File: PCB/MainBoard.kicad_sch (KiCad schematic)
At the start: 15 parts, among them U2 ATmega2560-16A, Y1 Crystal_GND24

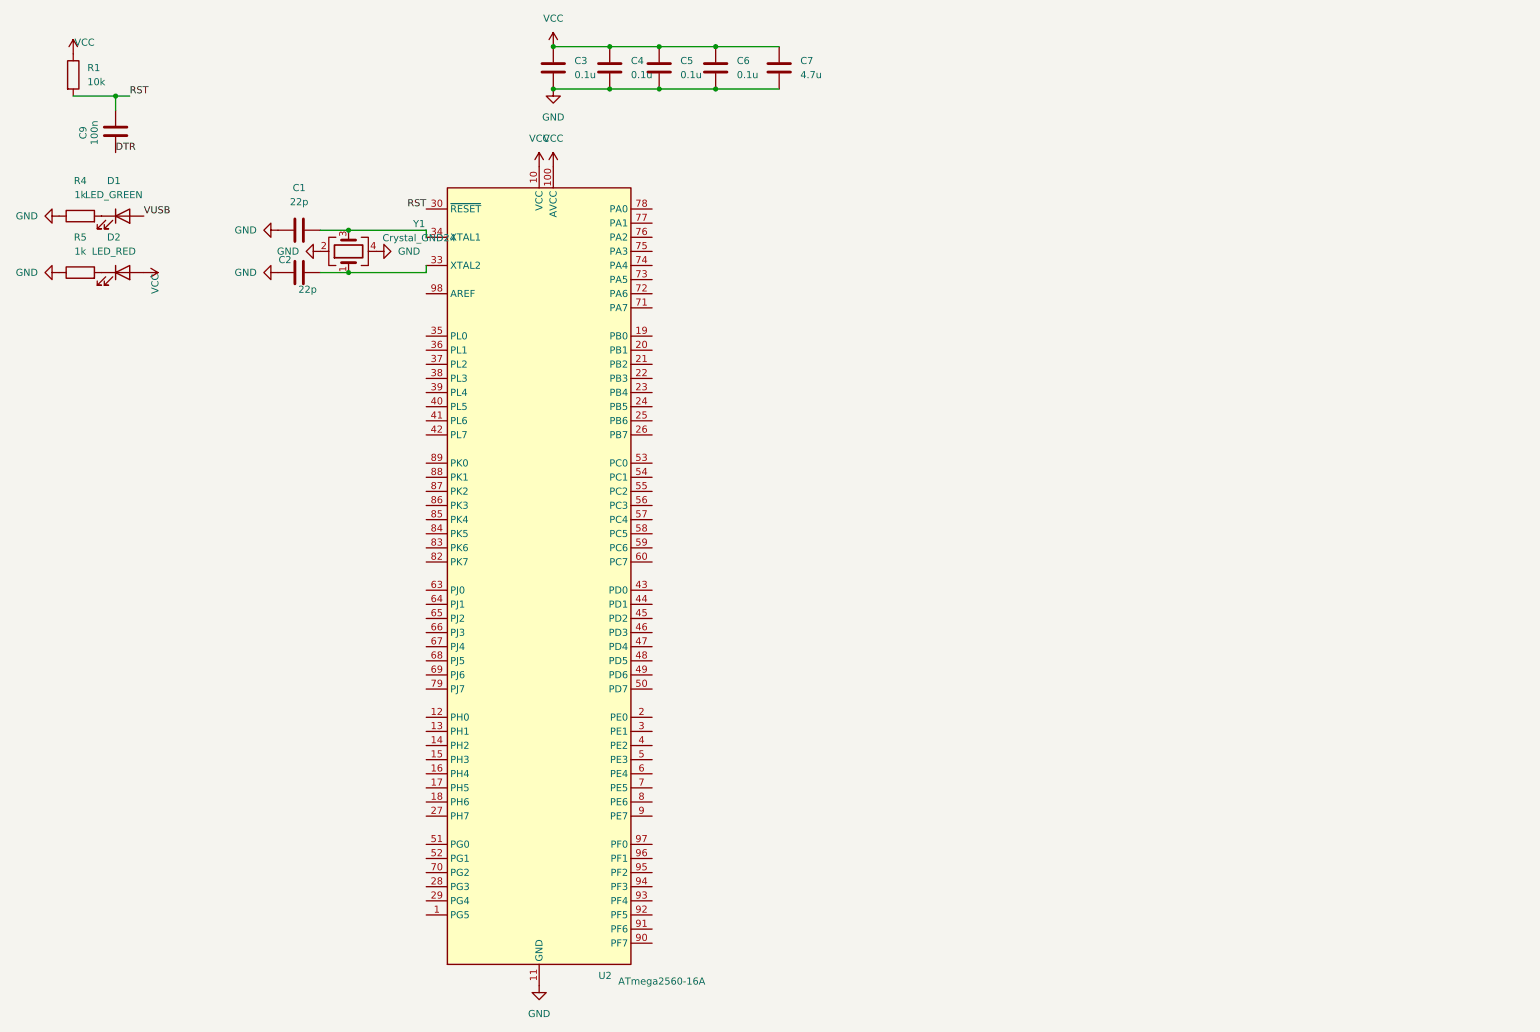
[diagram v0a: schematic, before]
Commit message: Updated board with the right hall effect analog sensor and some ADCs. Considering reducing the MCU.
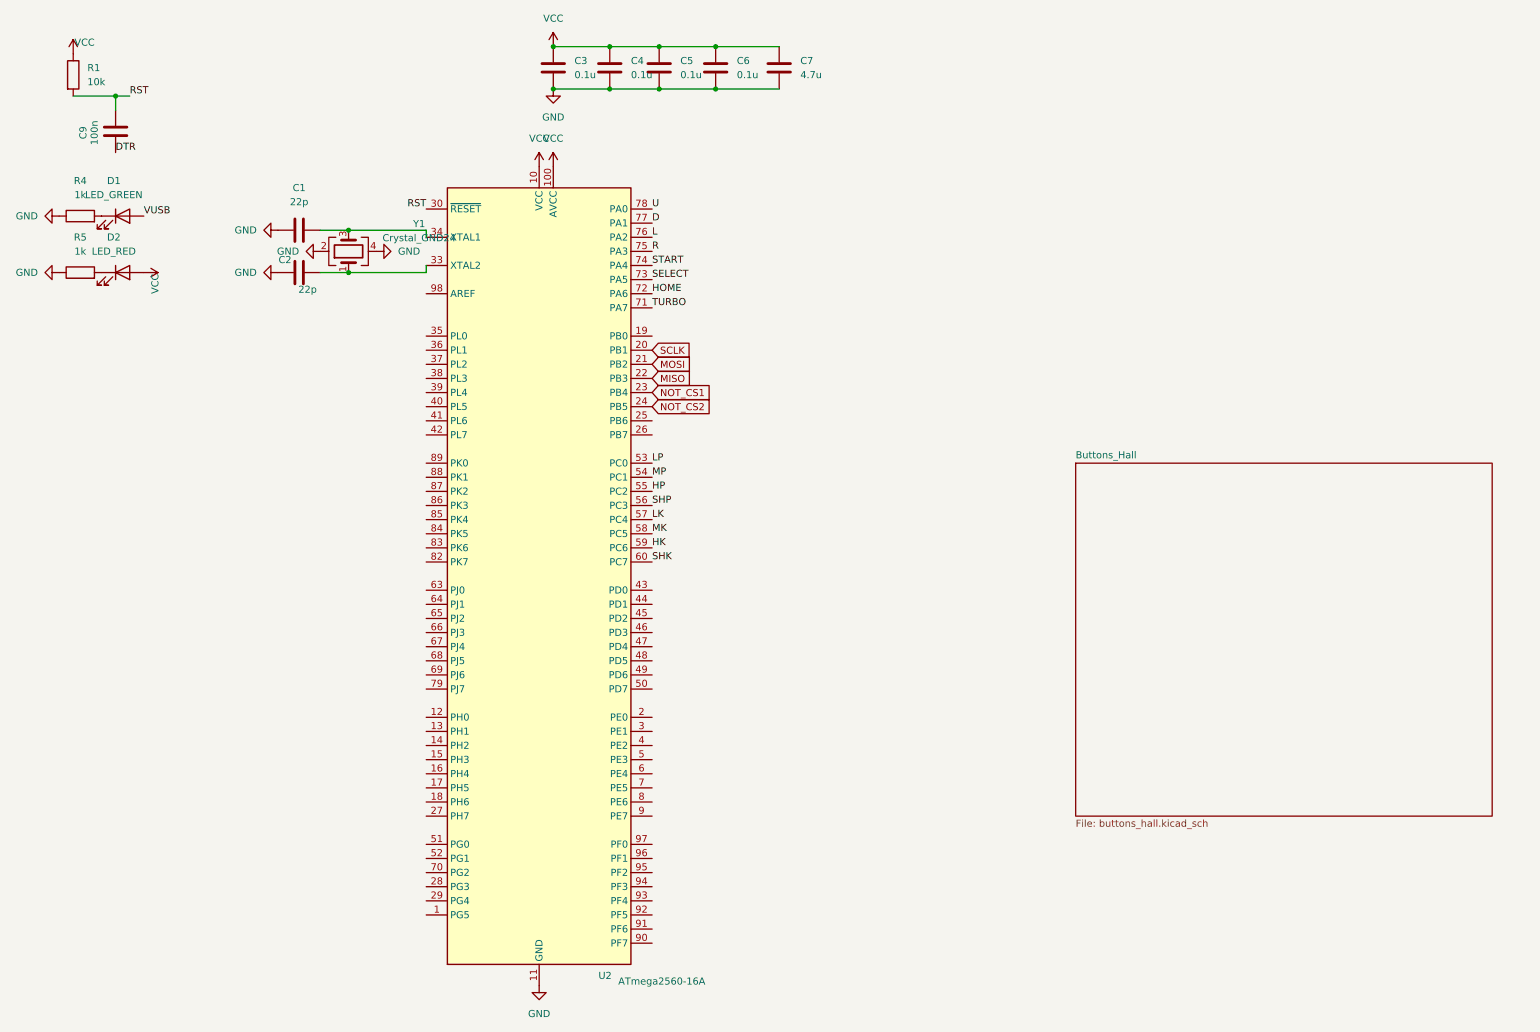
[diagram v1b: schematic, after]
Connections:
- net SCLK: now reaches U2.20 (PB1)
- net MOSI: now reaches U2.21 (PB2)
- net MISO: now reaches U2.22 (PB3)
- net NOT_CS1: now reaches U2.23 (PB4)
- net NOT_CS2: now reaches U2.24 (PB5)
- net LP: now reaches U2.53 (PC0)
- net MP: now reaches U2.54 (PC1)
- net HP: now reaches U2.55 (PC2)
- net SHP: now reaches U2.56 (PC3)
- net LK: now reaches U2.57 (PC4)
- net MK: now reaches U2.58 (PC5)
- net HK: now reaches U2.59 (PC6)
- net SHK: now reaches U2.60 (PC7)
- net TURBO: now reaches U2.71 (PA7)
- net HOME: now reaches U2.72 (PA6)
- net SELECT: now reaches U2.73 (PA5)
- net START: now reaches U2.74 (PA4)
- net R: now reaches U2.75 (PA3)
- net L: now reaches U2.76 (PA2)
- net D: now reaches U2.77 (PA1)
- net U: now reaches U2.78 (PA0)
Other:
- added sheet Buttons_Hall (buttons_hall.kicad_sch)

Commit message: Worked on schematic, added USB-C, worked on pcb
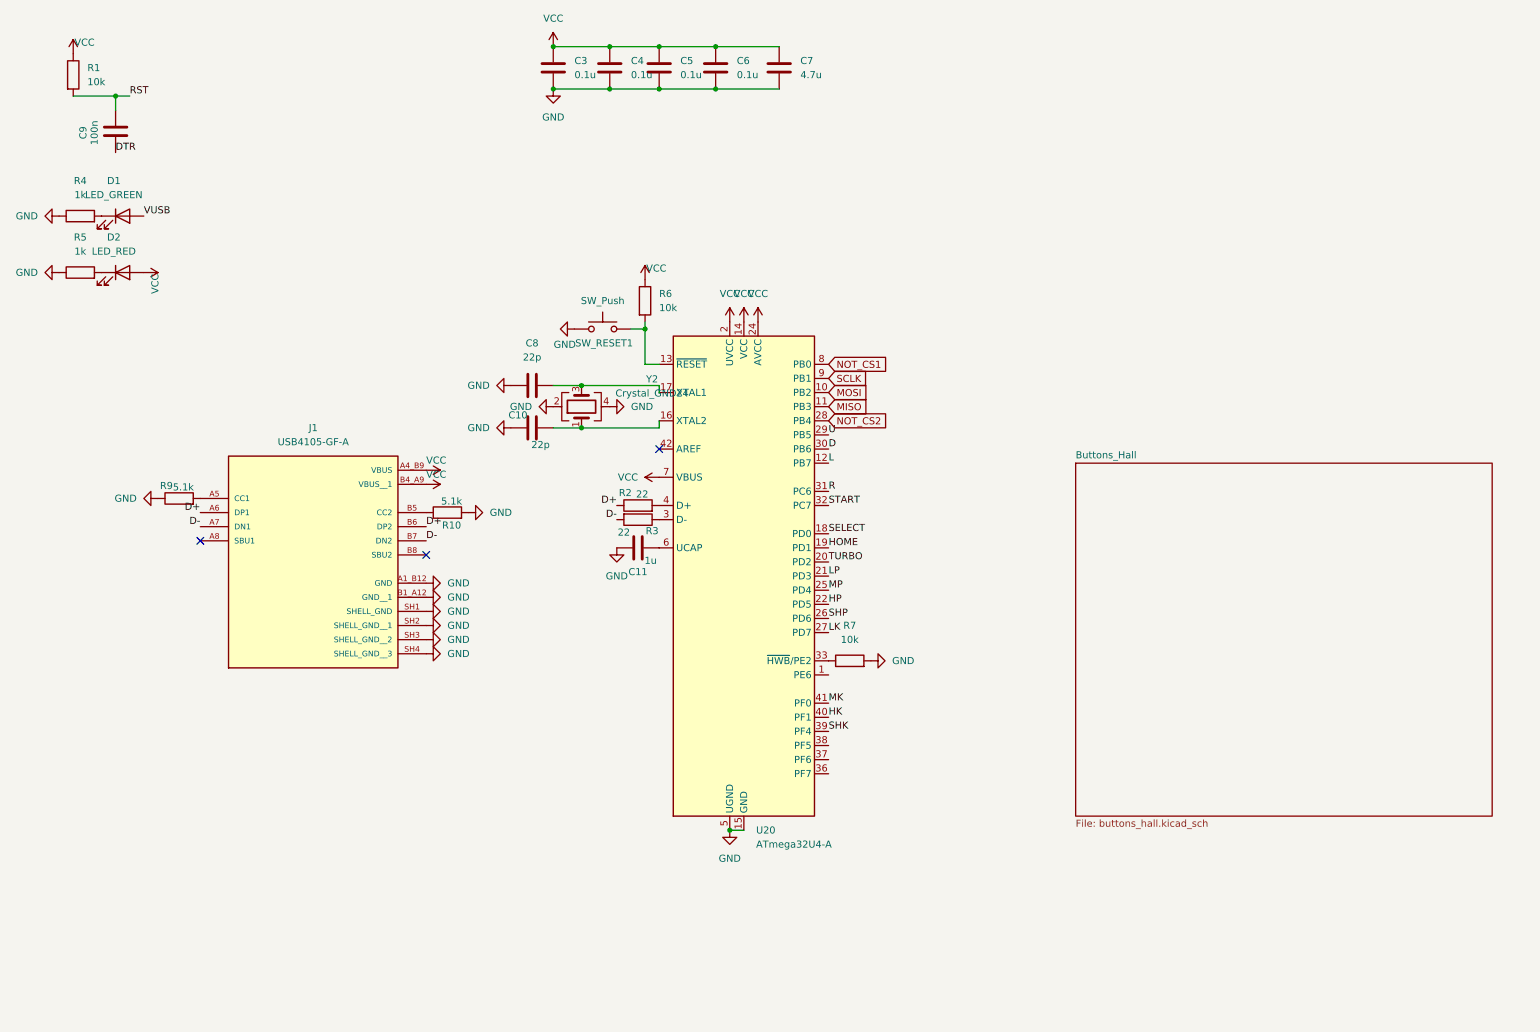
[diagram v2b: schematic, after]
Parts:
- removed C1, C2: 22p, Capacitor_SMD:C_0603_1608Metric, symbol Device:C
- removed U2: ATmega2560-16A, Package_QFP:TQFP-100_14x14mm_P0.5mm, symbol MCU_Microchip_ATmega:ATmega2560-16A
- removed Y1: Crystal_GND24, Crystal:Crystal_SMD_SeikoEpson_FA238-4Pin_3.2x2.5mm, symbol Device:Crystal_GND24
- added C10, C8: 22p, Capacitor_SMD:C_0603_1608Metric, symbol Device:C
- added C11: 1u, Capacitor_SMD:C_0603_1608Metric, symbol Device:C
- added J1: USB4105-GF-A, USB4105_GF_A:GCT_USB4105-GF-A, symbol USB4105-GF-A:USB4105-GF-A
- added R10, R9: 5.1k, Resistor_SMD:R_0603_1608Metric, symbol Device:R
- added R2, R3: 22, Resistor_SMD:R_0603_1608Metric, symbol Device:R
- added R6, R7: 10k, Resistor_SMD:R_0603_1608Metric, symbol Device:R
- added SW_RESET1: SW_Push, Button_Switch_SMD:SW_SPST_TL3342, symbol Switch:SW_Push
- added U20: ATmega32U4-A, Package_QFP:TQFP-44_10x10mm_P0.8mm, symbol MCU_Microchip_ATmega:ATmega32U4-A
- added Y2: Crystal_GND24, Crystal:Crystal_SMD_SeikoEpson_FA238-4Pin_3.2x2.5mm, symbol Device:Crystal_GND24
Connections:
- net D: now also U20.30 (PB6)
- net GND: now also C10.1, C11.1, C8.1, J1.A1_B12 (GND), J1.B1_A12 (GND__1), J1.SH1 (SHELL_GND), J1.SH2 (SHELL_GND__1), J1.SH3 (SHELL_GND__2), J1.SH4 (SHELL_GND__3), R10.2, R7.2, R9.1, SW_RESET1.1, U20.15 (GND), U20.23 (GND), U20.35 (GND), U20.43 (GND), U20.5 (UGND), Y2.2, Y2.4
- net HK: now also U20.40 (PF1)
- net HOME: now also U20.19 (PD1)
- net HP: now also U20.22 (PD5)
- net L: now also U20.12 (PB7)
- net LK: now also U20.27 (PD7)
- net LP: now also U20.21 (PD3)
- net MISO: now also U20.11 (PB3)
- net MK: now also U20.41 (PF0)
- net MOSI: now also U20.10 (PB2)
- net MP: now also U20.25 (PD4)
- net NOT_CS1: now also U20.8 (PB0)
- net NOT_CS2: now also U20.28 (PB4)
- net R: now also U20.31 (PC6)
- net SCLK: now also U20.9 (PB1)
- net SELECT: now also U20.18 (PD0)
- net SHK: now also U20.39 (PF4)
- net SHP: now also U20.26 (PD6)
- net START: now also U20.32 (PC7)
- net TURBO: now also U20.20 (PD2)
- net U: now also U20.29 (PB5)
- net VCC: now also J1.A4_B9 (VBUS), J1.B4_A9 (VBUS__1), R6.1, U20.14 (VCC), U20.2 (UVCC), U20.24 (AVCC), U20.34 (VCC), U20.44 (AVCC), U20.7 (VBUS)
- new net: C8.2, U20.17 (XTAL1), Y2.3
- new net: R6.2, SW_RESET1.2, U20.13 (~{RESET})
- new net: C10.2, U20.16 (XTAL2), Y2.1
- new net: R3.1, U20.3 (D-)
- new net: R7.1, U20.33 (~{HWB}/PE2)
- new net: R2.2, U20.4 (D+)
- new net: C11.2, U20.6 (UCAP)
- new net: J1.A5 (CC1), R9.2
- new net: J1.B5 (CC2), R10.1
- new net D+: J1.A6 (DP1), J1.B6 (DP2), R2.1
- new net D-: J1.A7 (DN1), J1.B7 (DN2), R3.2
- no-connect marks 0 -> 3

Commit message: Updated PCB and schematic with the Gateron footprint, added dummy Brooks footprint
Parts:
- added Brooks1: ~, BrooksBoards:BrooksP5Plus, symbol BrooksBoards:BrooksP5Plus
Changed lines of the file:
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@@
+	)
+	(symbol
+		(lib_id "BrooksBoards:BrooksP5Plus")
+		(at 222.25 53.34 0)
+		(unit 1)
+		(exclude_from_sim no)
+		(in_bom yes)
+		(on_board yes)
+		(dnp no)
+		(fields_autoplaced yes)
+		(property "Reference" "Brooks1"
+			(at 248.92 52.7049 0)
+			(effects
+				(font
+					(size 1.27 1.27)
+				)
+				(justify left)
+			)
+		)
+		(property "Value" "~"
+			(at 248.92 54.61 0)
+			(effects
+				(font
+					(size 1.27 1.27)
+				)
+				(justify left)
+			)
+		)
+		(property "Footprint" "BrooksBoards:BrooksP5Plus"
+			(at 222.25 53.34 0)
+			(effects
+				(font
+					(size 1.27 1.27)
+				)
+				(hide yes)
+			)
+		)
+		(property "Datasheet" ""
+			(at 222.25 53.34 0)
+			(effects
+				(font
+					(size 1.27 1.27)
+				)
+				(hide yes)
+			)
+		)
+		(property "Description" ""
+			(at 222.25 53.34 0)
+			(effects
+				(font
+					(size 1.27 1.27)
+				)
+				(hide yes)
+			)
+		)
+		(instances
+			(project ""
+				(path "/e015e616-37c3-4f95-aa49-76389b12ce2e"
+					(reference "Brooks1")
+					(unit 1)
+				)
+			)
+		)
 	)
 	(symbol

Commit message: Fallback Pico GP2040-CE added
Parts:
- removed C9: 100n, Capacitor_SMD:C_0603_1608Metric, symbol Device:C
- removed R1: 10k, Resistor_SMD:R_0603_1608Metric, symbol Device:R
- added U36: ~, BrooksBoards:BrooksP5Mini, symbol BrooksBoards:BrooksP5Mini
- added U37: Pico, MCU_RaspberryPi_and_Boards:RPi_Pico_SMD_TH, symbol MCU_RaspberryPi_and_Boards:Pico
